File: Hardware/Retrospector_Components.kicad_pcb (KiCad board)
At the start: 4 copper layers, 60 x 110 mm, 126 parts, among them J1 SWD_Header, J2 Eurorack_10_pin_power, J3 Conn_01x08_Male, J4 Conn_01x08_Male, J5 Conn_01x08_Male, J6 Conn_01x08_Male, J7 USB_B_Micro, U1 STM32H743ZITx, U2 IS42S16800F-7TLI, U3 PCM5100APW, U4 SSI2164, U5 MCP6004, U6 MCP6004, U7 TL074, U8 NCV1117DT33T5G, U9 BA7807FP-E2, Y1 8MHz 20pF

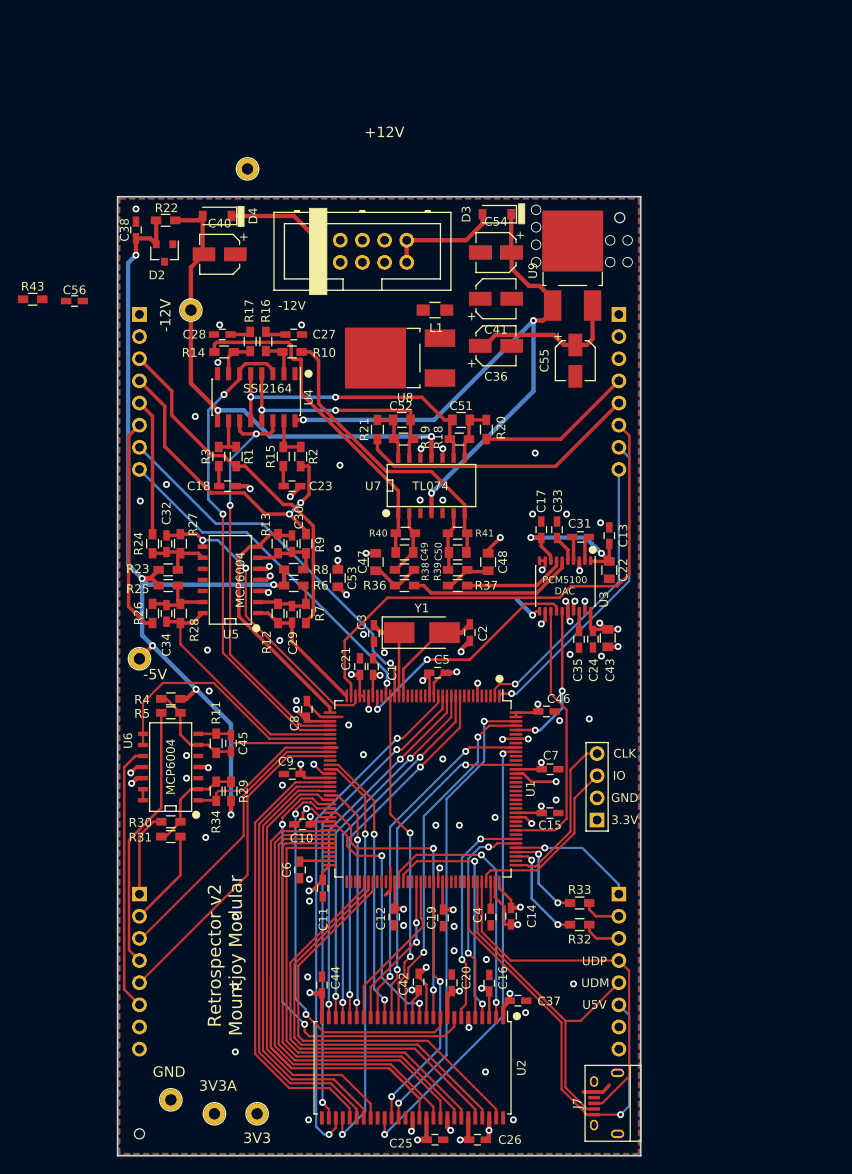
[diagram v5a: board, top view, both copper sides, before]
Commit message: Added Buck converter to PCB; other layout changes
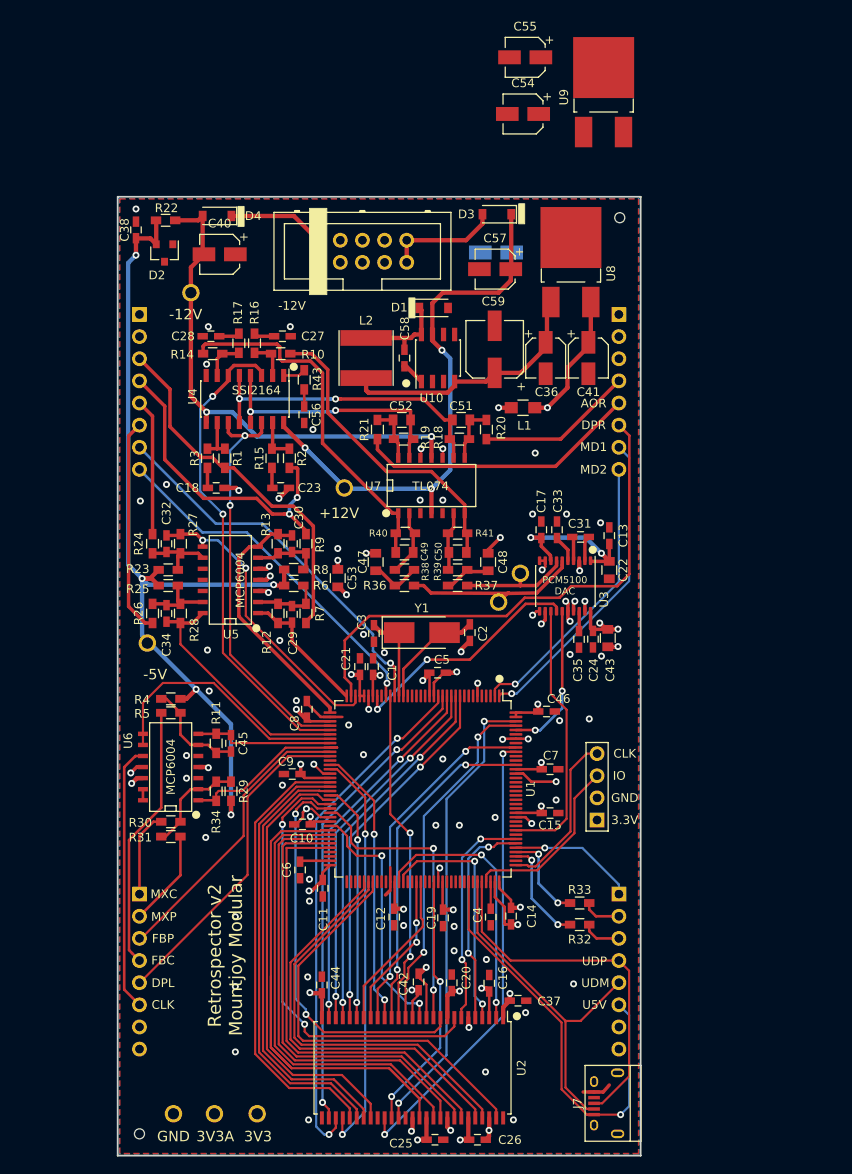
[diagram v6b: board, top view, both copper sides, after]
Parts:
- added C57: 22uF, Capacitors_SMD:CP_Elec_4x5.8, F.Cu at (143.3, 58.3)
- added C58: 10nF, Capacitors_SMD:C_0603_HandSoldering, F.Cu at (132.9, 68.5)
- added C59: 100uF, Capacitors_SMD:CP_Elec_6.3x5.8, F.Cu at (143.2, 67.5)
- added D1: 1N5819, Diodes_SMD:D_SOD-123, F.Cu at (136.2, 62.8)
- added L2: 68uH, Custom_Footprints:Inductor_SMD_6x6mm, F.Cu at (128.5, 68.5)
- added TP7: TestPoint, Custom_Footprints:1.3mm_Test_Point, F.Cu at (143.7, 96.5)
- added TP8: TestPoint, Custom_Footprints:1.3mm_Test_Point, F.Cu at (146.2, 93.2)
- added U10: LM2675M-5, Housings_SOIC:SOIC-8_3.9x4.9mm_Pitch1.27mm, F.Cu at (136.8, 68.5)
- C56: value 5nF -> 10nF
- moved TP5 38.2 mm to (126.0, 83.4)
- moved C55 35.3 mm to (146.8, 34.0), turned to 180 degrees
- moved R43 32.5 mm to (121.4, 71.0), turned to 90 degrees
- moved C56 29.4 mm to (121.4, 75.0), turned to 270 degrees
- moved U8 22.5 mm to (152.0, 57.5), turned to 90 degrees
- moved U9 20.2 mm to (155.8, 38.0)
- moved C54 16.2 mm to (146.5, 40.5)
- moved L1 15.1 mm to (146.5, 74.2)
- moved C41 12.6 mm to (154.0, 68.5), turned to 270 degrees
- moved C36 5.87 mm to (149.1, 68.5), turned to 270 degrees
- moved TP4 2.01 mm to (103.4, 101.2)
- moved TP6 2.00 mm to (108.4, 61.0)
- moved TP1 1.63 mm to (106.4, 155.2)
- moved U4 1.32 mm to (114.6, 73.2)
- moved C18 1.32 mm to (111.3, 83.4)
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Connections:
- net /+7V renamed /Int_V
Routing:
- net +3V3: track 88.6 -> 101.7 mm, vias 24 -> 25
- net /Int_V: track 18.0 -> 30.0 mm
- net VCC: track 75.5 -> 63.9 mm
- net Net-(C58-Pad1): track 0.00 -> 11.1 mm
- net Net-(C58-Pad2): track 0.00 -> 2.82 mm
- net Net-(R43-Pad2): track 0.00 -> 2.60 mm
- net AREF_-5: track 105.7 -> 103.6 mm, vias 6 -> 5
- net /DAC_OUT_AMP_L: track 39.4 -> 41.5 mm
- net Net-(C56-Pad1): track 0.00 -> 1.95 mm
- net /DAC_OUT_L: track 19.2 -> 20.9 mm
- net +3.3VA: track 27.7 -> 29.1 mm, vias 7 -> 8
- net /DAC_OUT_R: track 11.8 -> 13.2 mm
- net /DRY_OUT_R: track 28.2 -> 29.6 mm
- net /DRY_OUT_L: track 34.3 -> 35.5 mm
- net /DAC_OUT_AMP_R: track 34.5 -> 35.7 mm
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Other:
- board text added: "AOR"
- board text added: "CLK"
- board text added: "DPL"
- board text added: "DPR"
- board text added: "FBC"
- board text added: "FBP"
- board text added: "MD1"
- board text added: "MD2"
- board text added: "MXC"
- board text added: "MXP"

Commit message: Completed draft of rev 2 pcb
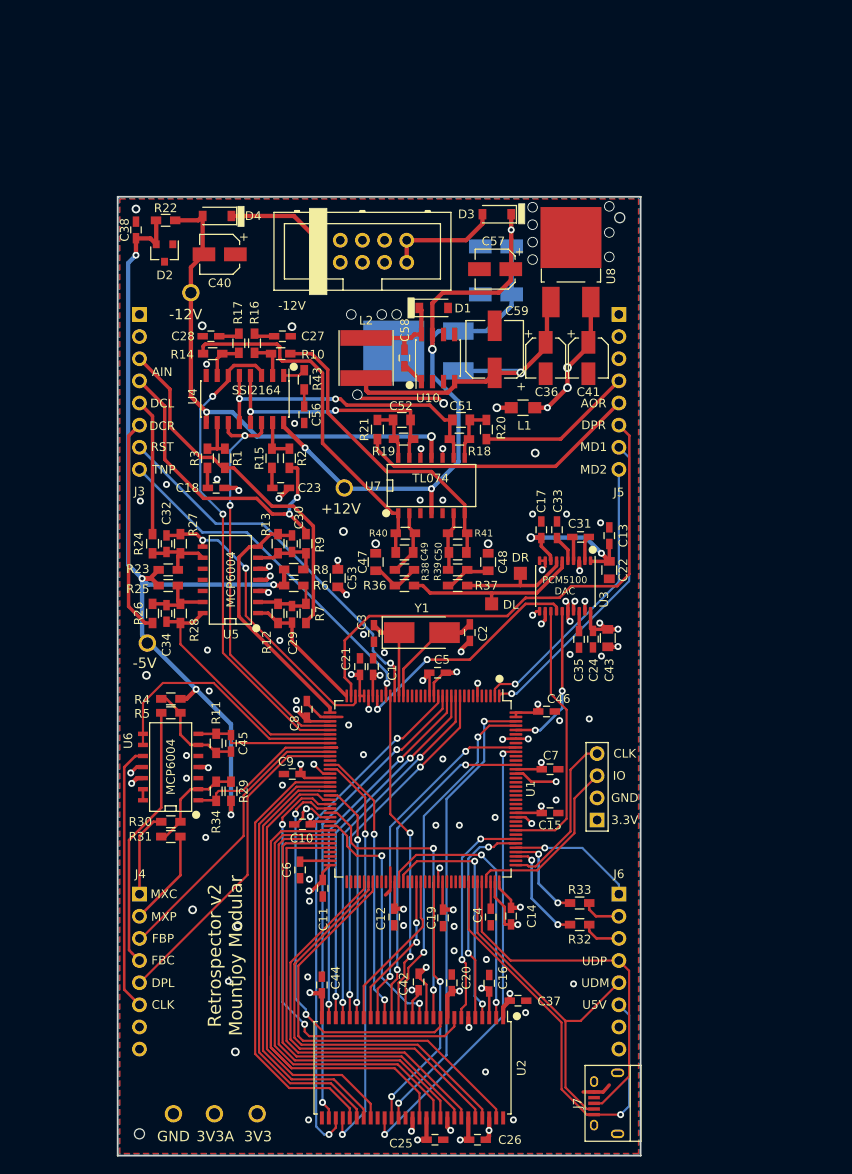
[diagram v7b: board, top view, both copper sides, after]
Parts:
- removed C55: 22uF, Capacitors_SMD:CP_Elec_4x5.8
- C54, U9: moved to B.Cu
- TP7, TP8: footprint Custom_Footprints:1.3mm_Test_Point -> Measurement_Points:Measurement_Point_Square-SMD-Pad_Small
- moved U9 36.5 mm to (134.5, 67.7), turned to 180 degrees
- moved C54 20.9 mm to (143.4, 61.2)
- moved TP7 0.82 mm to (142.9, 96.7)
- moved C39 0.70 mm to (143.4, 55.7)
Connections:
- net AREF_-5 renamed /-5V_REF
- net Net-(C58-Pad1) renamed /VSW
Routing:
- net VCC: track 63.9 -> 83.6 mm, vias 3 -> 4
- net /Int_V: track 30.0 -> 37.3 mm, vias 0 -> 1
- net GND: track 84.1 -> 91.2 mm, vias 83 -> 98
- net /FMC_D8: track 69.2 -> 64.5 mm
- net +3V3: vias 25 -> 27
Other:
- board text added: "AIN"
- board text added: "DCL"
- board text added: "DCR"
- board text added: "DL"
- board text added: "DR"
- board text added: "J3"
- board text added: "J4"
- board text added: "J5"
- board text added: "J6"
- board text added: "RST"
- board text added: "TNP"
